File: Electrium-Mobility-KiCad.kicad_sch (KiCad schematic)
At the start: 25 parts, among them M1 3V 75mA, Q1 NMOS, SW1 SW_Push, SW2 SW_Push, U1 ESP32-WROOM-32E, U2 LCD-016N002L, U3 TPB4056A20-ES1R

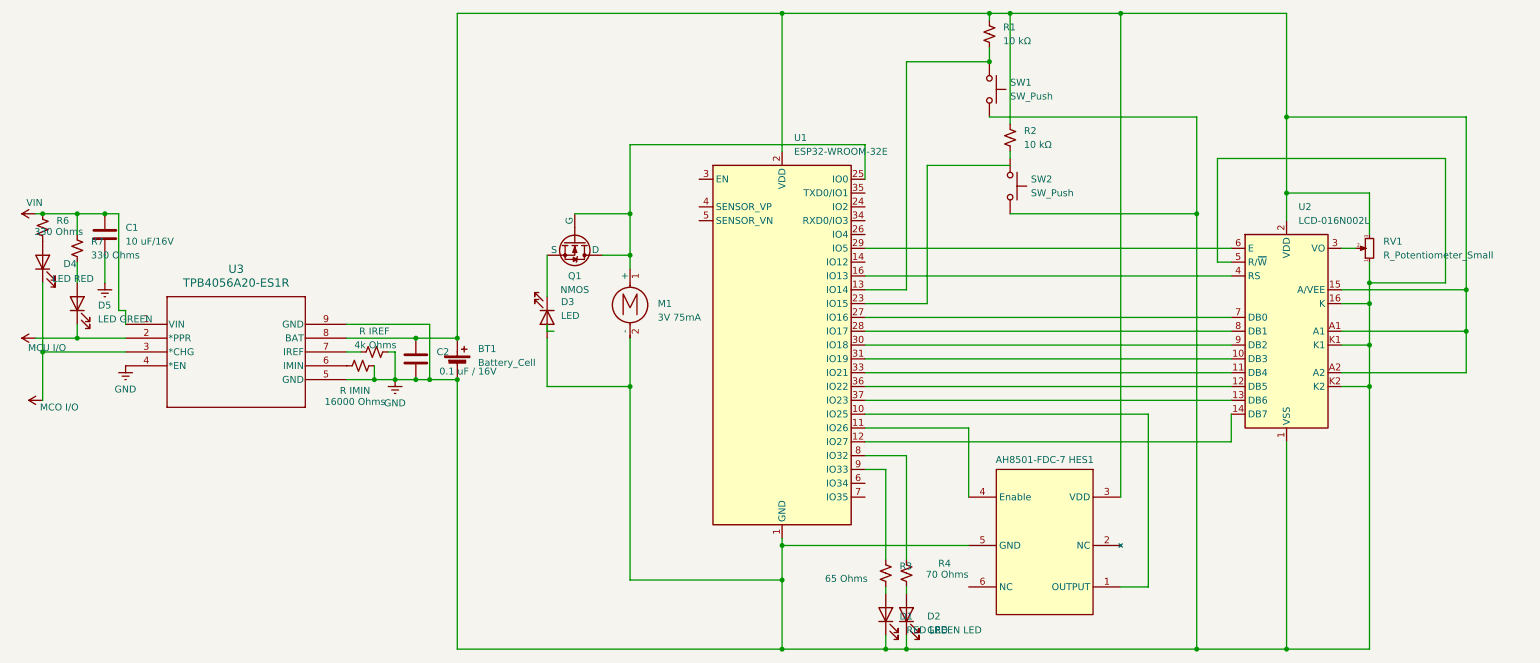
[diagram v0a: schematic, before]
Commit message: Updated hall effect sensor symbol
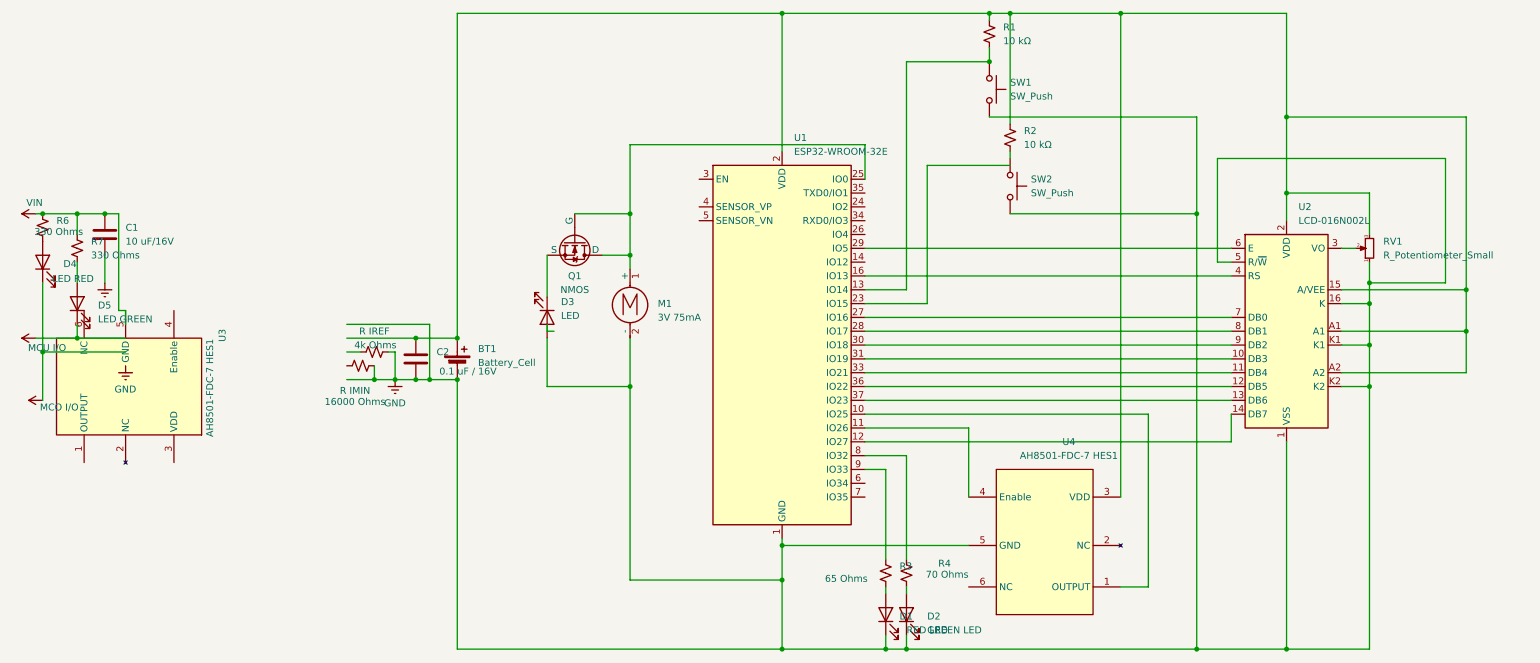
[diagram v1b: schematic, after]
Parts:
- removed AH8501-FDC-7 HES1: ~, symbol Sensor_Magnetic:AH8501-FDC-7
- added U4: AH8501-FDC-7 HES1, Library:6-UDFN, symbol Library:AH8501-FDC-7
- U3: value TPB4056A20-ES1R -> AH8501-FDC-7 HES1; footprint ESOP-8_TPK -> Library:6-UDFN
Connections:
- net GND: now also U4.5 (GND); no longer U3.4 (*EN), U3.5 (GND), U3.9 (GND)
- net MCO I/O: no longer U3.3 (*CHG)
- net MCU I/O: no longer U3.2 (*PPR)
- net VIN: now also U3.5 (GND); no longer U3.1 (VIN)
- net at U1.10 (IO25): now also U4.1 (OUTPUT)
- net at U1.11 (IO26): now also U4.4 (Enable)
- net at BT1.1 (+), C2.1, R1.1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: now also U4.3 (VDD); no longer U3.8 (BAT)
- net at R IMIN.1: no longer U3.6 (IMIN)
- net at R IREF.1: no longer U3.7 (IREF)
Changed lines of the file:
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@@
 	)
 	(symbol
-		(lib_id "Sensor_Magnetic:AH8501-FDC-7")
+		(lib_id "Device:R_Small_US")
+		(at 16.51 81.28 0)
+		(unit 1)
+		(exclude_from_sim no)
+		(in_bom yes)
+		(on_board yes)
+		(dnp no)
+		(property "Reference" "R6"
+			(at 19.05 80.0099 0)
+			(effects
+				(font
+					(size 1.27 1.27)
+				)
+				(justify left)
+			)
+		)
+		(property "Value" "330 Ohms"
+			(at 14.986 82.042 0)
+			(effects
+				(font
+					(size 1.27 1.27)
+				)
+				(justify left)
+			)
+		)
+		(property "Footprint" ""
+			(at 16.51 81.28 0)
+			(effects
+				(font
+					(size 1.27 1.27)
+				)
+				(hide yes)
+			)
+		)
+		(property "Datasheet" "~"
+			(at 16.51 81.28 0)
+			(effects
+				(font
+					(size 1.27 1.27)
+				)
+				(hide yes)
+			)
+		)
+		(property "Description" "Resistor, small US symbol"
+			(at 16.51 81.28 0)
+			(effects
+				(font
+					(size 1.27 1.27)
+				)
+				(hide yes)
+			)
+		)
+		(pin "2"
+		)
+		(pin "1"
+		)
+		(instances
+			(project ""
+				(path "/77cfd6b1-cf11-45d1-96c8-b00f1af024ba"
+					(reference "R6")
+					(unit 1)
+				)
+			)
+		)
+	)
+	(symbol
+		(lib_id "Device:LED")
+		(at 16.51 87.63 90)
+		(unit 1)
+		(exclude_from_sim no)
+		(in_bom yes)
+		(on_board yes)
+		(dnp no)
+		(property "Reference" "D4"
+			(at 20.32 87.9474 90)
+			(effects
+				(font
+					(size 1.27 1.27)
+				)
+				(justify right)
+			)
+		)
+		(property "Value" "LED RED"
+			(at 18.288 90.678 90)
+			(effects
+				(font
+					(size 1.27 1.27)
+				)
+				(justify right)
+			)
+		)
+		(property "Footprint" ""
+			(at 16.51 87.63 0)
+			(effects
+				(font
+					(size 1.27 1.27)
+				)
+				(hide yes)
+			)
+		)
+		(property "Datasheet" "~"
+			(at 16.51 87.63 0)
+			(effects
+				(font
+					(size 1.27 1.27)
+				)
+				(hide yes)
+			)
+		)
+		(property "Description" "Light emitting diode"
+			(at 16.51 87.63 0)
+			(effects
+				(font
+					(size 1.27 1.27)
+				)
+				(hide yes)
+			)
+		)
+		(pin "2"
+		)
+		(pin "1"
+		)
+		(instances
+			(project ""
+				(path "/77cfd6b1-cf11-45d1-96c8-b00f1af024ba"
+					(reference "D4")
+					(unit 1)
+				)
+			)
+		)
+	)
+	(symbol
+		(lib_id "Library:AH8501-FDC-7")
 		(at 189.23 139.7 90)
 		(unit 1)
@@
 		(on_board yes)
 		(dnp no)
-		(property "Reference" "AH8501-FDC-7 HES1"
-			(at 200.66 123.952 90)
-			(effects
-				(font
-					(size 1.27 1.27)
-				)
-			)
-		)
-		(property "Value" "~"
-			(at 205.105 124.46 90)
-			(effects
-				(font
-					(size 1.27 1.27)
-				)
-			)
-		)
-		(property "Footprint" ""
+		(fields_autoplaced yes)
+		(property "Reference" "U4"
+			(at 205.105 120.65 90)
+			(effects
+				(font
+					(size 1.27 1.27)
+				)
+			)
+		)
+		(property "Value" "AH8501-FDC-7 HES1"
+			(at 205.105 123.19 90)
+			(effects
+				(font
+					(size 1.27 1.27)
+				)
+			)
+		)
+		(property "Footprint" "Library:6-UDFN"
 			(at 186.69 139.7 0)
 			(effects
@@
 			)
 		)
-		(pin "1"
+		(pin "4"
+		)
+		(pin "3"
+		)
+		(pin "5"
+		)
+		(pin "2"
 		)
 		(pin "6"
 		)
-		(pin "2"
-		)
-		(pin "3"
-		)
-		(pin "4"
-		)
-		(pin "5"
-		)
-		(instances
-			(project ""
-				(path "/77cfd6b1-cf11-45d1-96c8-b00f1af024ba"
-					(reference "AH8501-FDC-7 HES1")
-					(unit 1)
-				)
-			)
-		)
-	)
-	(symbol
-		(lib_id "Device:R_Small_US")
-		(at 16.51 81.28 0)
-		(unit 1)
-		(exclude_from_sim no)
-		(in_bom yes)
-		(on_board yes)
-		(dnp no)
-		(property "Reference" "R6"
-			(at 19.05 80.0099 0)
-			(effects
-				(font
-					(size 1.27 1.27)
-				)
-				(justify left)
-			)
-		)
-		(property "Value" "330 Ohms"
-			(at 14.986 82.042 0)
-			(effects
-				(font
-					(size 1.27 1.27)
-				)
-				(justify left)
-			)
-		)
-		(property "Footprint" ""
-			(at 16.51 81.28 0)
-			(effects
-				(font
-					(size 1.27 1.27)
-				)
-				(hide yes)
-			)
-		)
-		(property "Datasheet" "~"
-			(at 16.51 81.28 0)
-			(effects
-				(font
-					(size 1.27 1.27)
-				)
-				(hide yes)
-			)
-		)
-		(property "Description" "Resistor, small US symbol"
-			(at 16.51 81.28 0)
-			(effects
-				(font
-					(size 1.27 1.27)
-				)
-				(hide yes)
-			)
-		)
-		(pin "2"
-		)
-		(pin "1"
-		)
-		(instances
-			(project ""
-				(path "/77cfd6b1-cf11-45d1-96c8-b00f1af024ba"
-					(reference "R6")
-					(unit 1)
-				)
-			)
-		)
-	)
-	(symbol
-		(lib_id "Device:LED")
-		(at 16.51 87.63 90)
-		(unit 1)
-		(exclude_from_sim no)
-		(in_bom yes)
-		(on_board yes)
-		(dnp no)
-		(property "Reference" "D4"
-			(at 20.32 87.9474 90)
-			(effects
-				(font
-					(size 1.27 1.27)
-				)
-				(justify right)
-			)
-		)
-		(property "Value" "LED RED"
-			(at 18.288 90.678 90)
-			(effects
-				(font
-					(size 1.27 1.27)
-				)
-				(justify right)
-			)
-		)
-		(property "Footprint" ""
-			(at 16.51 87.63 0)
-			(effects
-				(font
-					(size 1.27 1.27)
-				)
-				(hide yes)
-			)
-		)
-		(property "Datasheet" "~"
-			(at 16.51 87.63 0)
-			(effects
-				(font
-					(size 1.27 1.27)
-				)
-				(hide yes)
-			)
-		)
-		(property "Description" "Light emitting diode"
-			(at 16.51 87.63 0)
-			(effects
-				(font
-					(size 1.27 1.27)
-				)
-				(hide yes)
-			)
-		)
-		(pin "2"
-		)
-		(pin "1"
-		)
-		(instances
-			(project ""
-				(path "/77cfd6b1-cf11-45d1-96c8-b00f1af024ba"
-					(reference "D4")
+		(pin "1"
+		)
+		(instances
+			(project ""
+				(path "/77cfd6b1-cf11-45d1-96c8-b00f1af024ba"
+					(reference "U4")
 					(unit 1)
 				)
@@
 		(fields_autoplaced yes)
 		(property "Reference" "U3"
-			(at 52.07 88.9 0)
-			(effects
-				(font
-					(size 1.524 1.524)
-				)
-			)
-		)
-		(property "Value" "TPB4056A20-ES1R"
-			(at 52.07 91.44 0)
-			(effects
-				(font
-					(size 1.524 1.524)
-				)
-			)
-		)
-		(property "Footprint" "ESOP-8_TPK"
-			(at 31.75 99.06 0)
-			(effects
-				(font
-					(size 1.27 1.27)
-					(italic yes)
-				)
-				(hide yes)
-			)
-		)
-		(property "Datasheet" "TPB4056A20-ES1R"
-			(at 31.75 99.06 0)
-			(effects
-				(font
-					(size 1.27 1.27)
-					(italic yes)
+			(at 49.53 101.092 90)
+			(effects
+				(font
+					(size 1.27 1.27)
+				)
+			)
+		)
+		(property "Value" "AH8501-FDC-7 HES1"
+			(at 47.244 110.744 90)
+			(effects
+				(font
+					(size 1.27 1.27)
+				)
+			)
+		)
+		(property "Footprint" "Library:6-UDFN"
+			(at 31.75 96.52 0)
+			(effects
+				(font
+					(size 1.27 1.27)
+				)
+				(hide yes)
+			)
+		)
+		(property "Datasheet" ""
+			(at 31.75 96.52 0)
+			(effects
+				(font
+					(size 1.27 1.27)
 				)
 				(hide yes)
@@
 		)
 		(property "Description" ""
-			(at 31.75 99.06 0)
+			(at 31.75 96.52 0)
 			(effects
 				(font
@@
 		(pin "6"
 		)
-		(pin "7"
-		)
-		(pin "8"
-		)
 		(pin "2"
 		)
@@
 		(pin "1"
 		)
-		(pin "9"
-		)
 		(pin "3"
